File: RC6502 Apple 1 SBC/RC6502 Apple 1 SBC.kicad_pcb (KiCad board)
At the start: 2 copper layers, 99.1 x 99.7 mm, 48 parts, among them J1 VP GND, J10 RAM_EN, J11 PIA_EN, J2 Arduino Nano, J3 Backplane, J4 Hole, J5 Hole, J6 Hole, J7 Hole, J8 Power, J9 ROM_EN, SW1 RESET, U1 WD65C02, U2 HM62256BLP-7, U3 74HCT138, U4 28C256, U5 74HCT00, U6 NE555, U7 74HCT04, U8 WD65C21, U9 MCP23S17, X1 1MHz

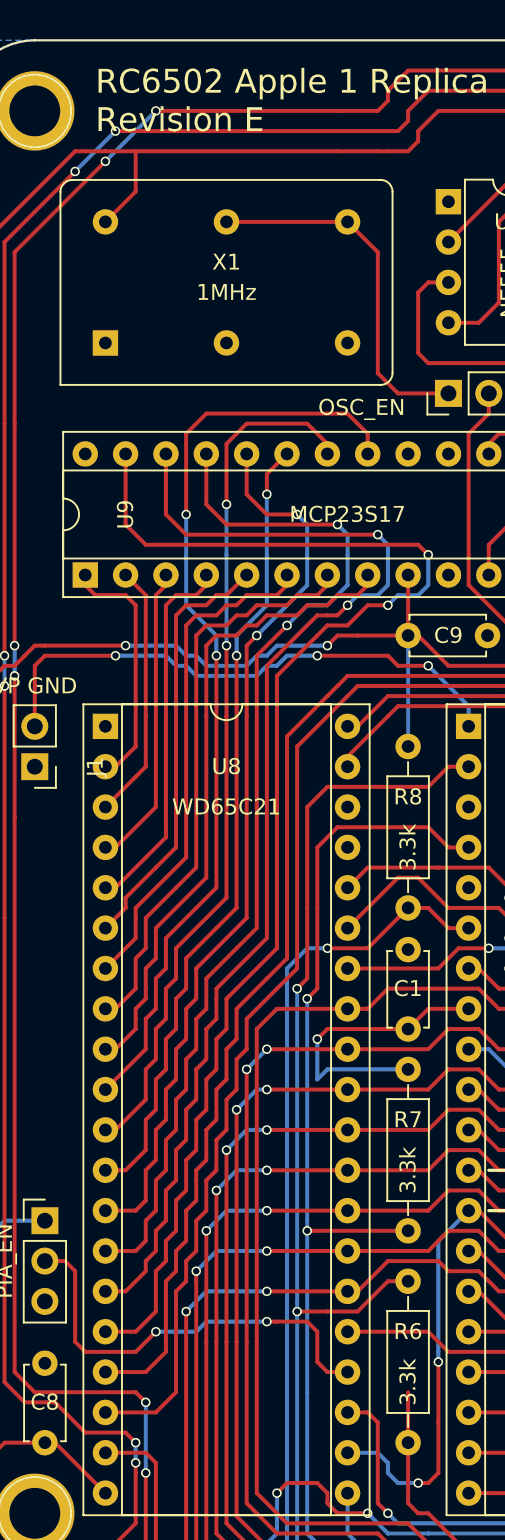
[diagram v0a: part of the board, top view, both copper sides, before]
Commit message: SBC revision E was missing VCC to CPU for some reason
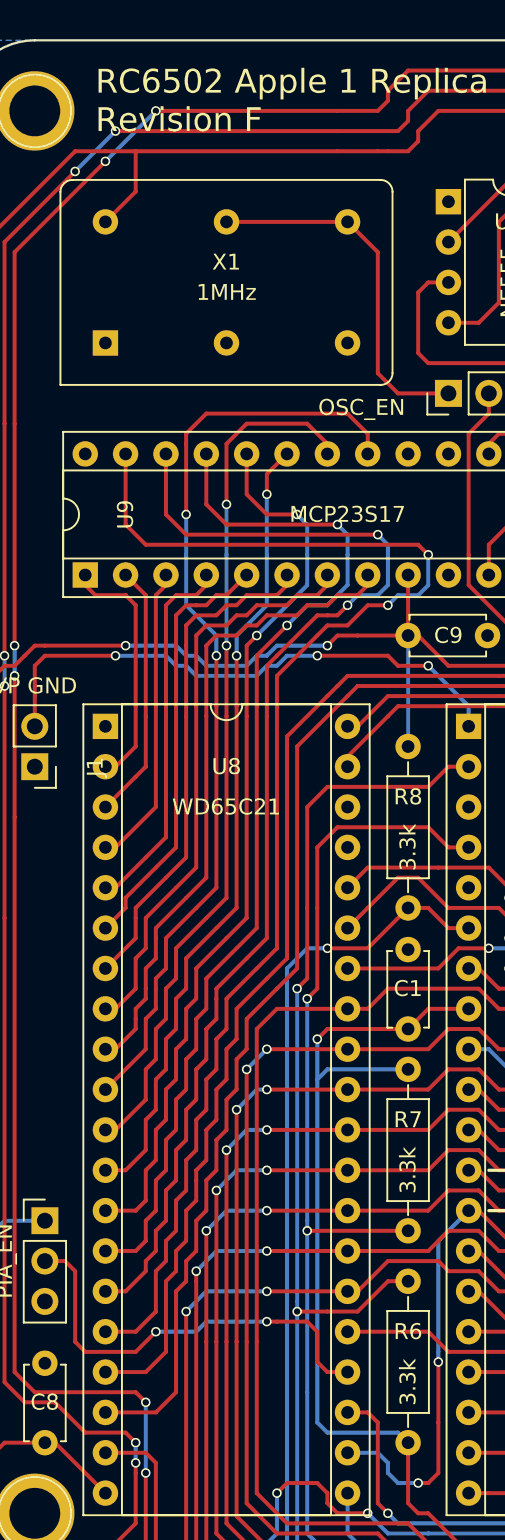
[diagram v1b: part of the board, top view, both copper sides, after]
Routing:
- net VCC: track 643.9 -> 668.5 mm
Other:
- board text added: "RC6502 Apple 1 Replica Revision F"
- board text removed: "RC6502 Apple 1 Replica Revision E"
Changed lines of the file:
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@@
   (general
     (links 240)
-    (no_connects 1)
+    (no_connects 0)
     (area 114.23 35.22 220.820001 148.420001)
     (thickness 1.6)
     (drawings 168)
-    (tracks 2242)
+    (tracks 2245)
     (zones 0)
     (modules 48)
@@
     (effects (font (size 1 1) (thickness 0.15)))
   )
-  (gr_text "RC6502 Apple 1 Replica\nRevision E" (at 124.46 43.18) (layer F.SilkS)
+  (gr_text "RC6502 Apple 1 Replica\nRevision F" (at 124.46 43.18) (layer F.SilkS)
     (effects (font (size 1.5 1.5) (thickness 0.3)) (justify left))
   )
@@
   (segment (start 189.865 67.31) (end 191.135 66.04) (width 0.25) (layer F.Cu) (net 2))
   (segment (start 191.135 66.04) (end 191.135 65.405) (width 0.25) (layer F.Cu) (net 2))
+  (segment (start 138.43 104.775) (end 138.43 126.365) (width 0.25) (layer B.Cu) (net 3))
+  (segment (start 143.51 127) (end 144.145 127.635) (width 0.25) (layer B.Cu) (net 3))
+  (segment (start 139.065 127) (end 143.51 127) (width 0.25) (layer B.Cu) (net 3))
+  (segment (start 138.43 126.365) (end 139.065 127) (width 0.25) (layer B.Cu) (net 3))
   (segment (start 157.48 48.895) (end 158.75 48.895) (width 0.25) (layer F.Cu) (net 3))
   (segment (start 158.75 48.895) (end 164.465 43.18) (width 0.25) (layer F.Cu) (net 3))
@@
   (segment (start 119.38 78.74) (end 118.745 78.74) (width 0.25) (layer F.Cu) (net 3))
   (segment (start 144.145 127.635) (end 144.145 131.445) (width 0.25) (layer F.Cu) (net 3))
-  (segment (start 145.415 132.08) (end 149.225 135.89) (width 0.25) (layer F.Cu) (net 3))
-  (via (at 149.225 135.89) (size 0.6) (drill 0.4) (layers F.Cu B.Cu) (net 3))
-  (segment (start 144.145 131.445) (end 144.78 132.08) (width 0.25) (layer F.Cu) (net 3))
   (segment (start 144.78 132.08) (end 145.415 132.08) (width 0.25) (layer F.Cu) (net 3))
+  (segment (start 144.145 131.445) (end 144.78 132.08) (width 0.25) (layer F.Cu) (net 3))
+  (via (at 149.225 135.89) (size 0.6) (drill 0.4) (layers F.Cu B.Cu) (net 3))
+  (segment (start 145.415 132.08) (end 149.225 135.89) (width 0.25) (layer F.Cu) (net 3))
   (segment (start 174.625 132.715) (end 177.8 132.715) (width 0.25) (layer F.Cu) (net 3))
   (via (at 178.435 134.62) (size 0.6) (drill 0.4) (layers F.Cu B.Cu) (net 3))
@@
   (via (at 138.43 102.235) (size 0.6) (drill 0.4) (layers F.Cu B.Cu) (net 3))
   (segment (start 138.43 102.235) (end 139.065 101.6) (width 0.25) (layer F.Cu) (net 3))
-  (segment (start 144.145 127.635) (end 144.145 124.46) (width 0.25) (layer F.Cu) (net 3))
   (segment (start 144.145 101.6) (end 145.415 100.33) (width 0.25) (layer F.Cu) (net 3))
   (segment (start 145.415 100.33) (end 147.955 100.33) (width 0.25) (layer F.Cu) (net 3))

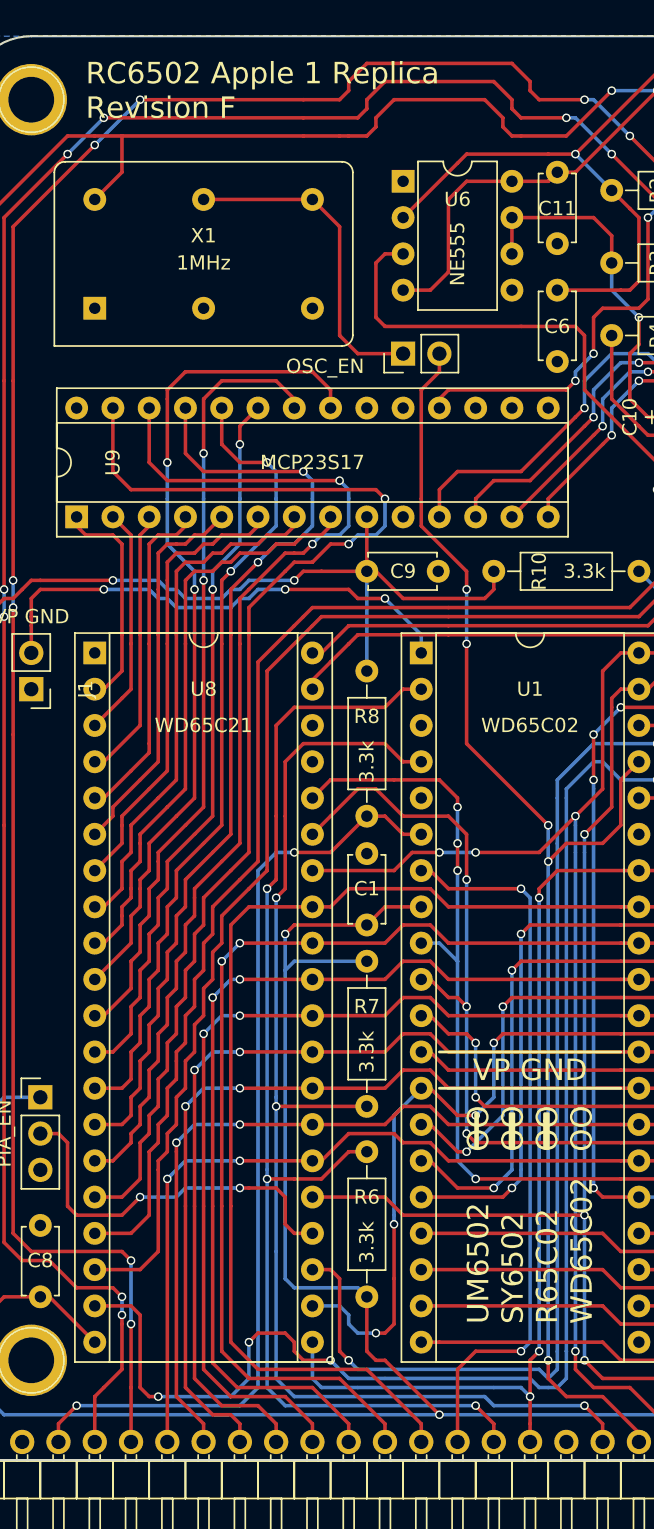
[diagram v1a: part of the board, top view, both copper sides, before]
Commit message: Added Phi1 to backplane connector
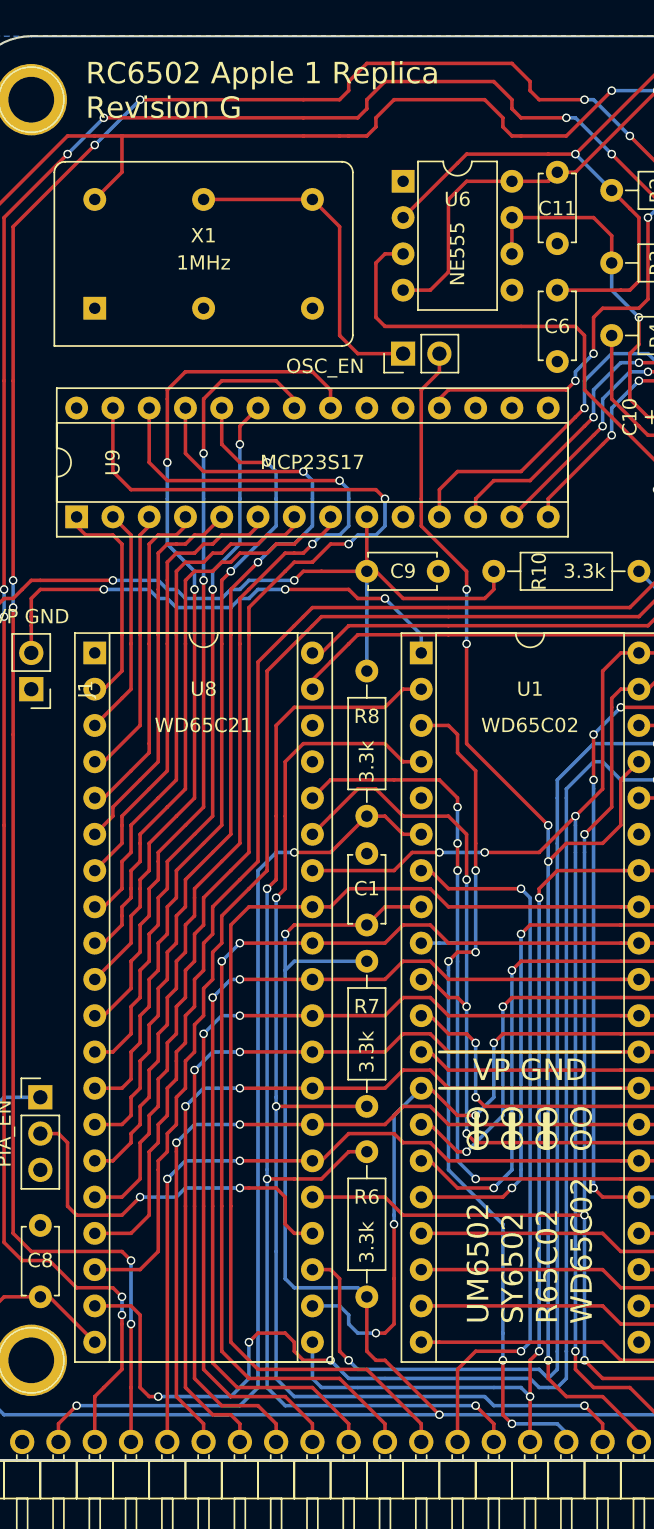
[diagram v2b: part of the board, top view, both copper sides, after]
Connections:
- J3 pad 23: (no net) -> PHI1
- U1 pad 3: (no net) -> PHI1
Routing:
- net PHI1: track 0.00 -> 59.7 mm, vias 0 -> 5
- net A0: track 118.0 -> 117.4 mm
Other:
- board text added: "RC6502 Apple 1 Replica Revision G"
- board text removed: "RC6502 Apple 1 Replica Revision F"
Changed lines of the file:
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@@
 (kicad_pcb (version 4) (host pcbnew 4.0.7)
   (general
-    (links 240)
+    (links 241)
     (no_connects 0)
-    (area 114.23 35.22 220.820001 148.420001)
+    (area 116.129999 39.294999 215.340001 139.140001)
     (thickness 1.6)
     (drawings 168)
-    (tracks 2245)
+    (tracks 2270)
     (zones 0)
     (modules 48)
-    (nets 84)
+    (nets 85)
   )
   (page A4)
@@
   (net 82 "Net-(J11-Pad2)")
   (net 83 "Net-(JP1-Pad1)")
+  (net 84 PHI1)
   (net_class Default "This is the default net class."
     (clearance 0.2)
@@
     (add_net OUT_DA)
     (add_net OUT_RDA)
+    (add_net PHI1)
     (add_net PHI2)
     (add_net P_RESET)
@@
     (pad 22 thru_hole oval (at 15.24 45.72) (size 1.6 1.6) (drill 0.8) (layers *.Cu *.Mask)
       (net 19 A12))
-    (pad 3 thru_hole oval (at 0 5.08) (size 1.6 1.6) (drill 0.8) (layers *.Cu *.Mask))
+    (pad 3 thru_hole oval (at 0 5.08) (size 1.6 1.6) (drill 0.8) (layers *.Cu *.Mask)
+      (net 84 PHI1))
     (pad 23 thru_hole oval (at 15.24 43.18) (size 1.6 1.6) (drill 0.8) (layers *.Cu *.Mask)
       (net 18 A13))
@@
     (pad 22 thru_hole oval (at 0 53.34 270) (size 1.7 1.7) (drill 1) (layers *.Cu *.Mask)
       (net 35 IRQ))
-    (pad 23 thru_hole oval (at 0 55.88 270) (size 1.7 1.7) (drill 1) (layers *.Cu *.Mask))
+    (pad 23 thru_hole oval (at 0 55.88 270) (size 1.7 1.7) (drill 1) (layers *.Cu *.Mask)
+      (net 84 PHI1))
     (pad 24 thru_hole oval (at 0 58.42 270) (size 1.7 1.7) (drill 1) (layers *.Cu *.Mask)
       (net 36 RW))
@@
     (effects (font (size 1 1) (thickness 0.15)))
   )
-  (gr_text "RC6502 Apple 1 Replica\nRevision F" (at 124.46 43.18) (layer F.SilkS)
+  (gr_text "RC6502 Apple 1 Replica\nRevision G" (at 124.46 43.18) (layer F.SilkS)
     (effects (font (size 1.5 1.5) (thickness 0.3)) (justify left))
   )
@@
   (segment (start 175.895 116.205) (end 182.245 116.205) (width 0.25) (layer F.Cu) (net 30))
   (via (at 175.895 116.205) (size 0.6) (drill 0.4) (layers F.Cu B.Cu) (net 30))
+  (segment (start 149.225 102.87) (end 150.495 102.87) (width 0.25) (layer B.Cu) (net 31))
   (segment (start 194.31 128.27) (end 194.31 130.175) (width 0.25) (layer B.Cu) (net 31))
   (segment (start 189.23 132.08) (end 190.5 130.81) (width 0.25) (layer F.Cu) (net 31))
@@
   (segment (start 178.435 117.475) (end 189.865 117.475) (width 0.25) (layer F.Cu) (net 31))
   (segment (start 150.495 97.79) (end 150.495 95.885) (width 0.25) (layer F.Cu) (net 31))
-  (segment (start 150.495 92.71) (end 149.225 91.44) (width 0.25) (layer F.Cu) (net 31))
-  (segment (start 149.225 91.44) (end 146.05 91.44) (width 0.25) (layer F.Cu) (net 31))
-  (segment (start 141.605 91.44) (end 146.05 91.44) (width 0.25) (layer F.Cu) (net 31))
-  (segment (start 140.335 92.71) (end 141.605 91.44) (width 0.25) (layer F.Cu) (net 31))
-  (segment (start 150.495 97.79) (end 150.495 104.14) (width 0.25) (layer B.Cu) (net 31))
-  (via (at 150.495 97.79) (size 0.6) (drill 0.4) (layers F.Cu B.Cu) (net 31))
-  (segment (start 150.495 93.345) (end 150.495 92.71) (width 0.25) (layer F.Cu) (net 31))
-  (via (at 150.495 93.345) (size 0.6) (drill 0.4) (layers F.Cu B.Cu) (net 31))
-  (segment (start 150.495 95.885) (end 150.495 93.345) (width 0.25) (layer B.Cu) (net 31))
   (via (at 150.495 95.885) (size 0.6) (drill 0.4) (layers F.Cu B.Cu) (net 31))
+  (segment (start 150.495 95.885) (end 150.495 93.345) (width 0.25) (layer B.Cu) (net 31))
+  (via (at 150.495 93.345) (size 0.6) (drill 0.4) (layers F.Cu B.Cu) (net 31))
+  (segment (start 150.495 93.345) (end 150.495 92.71) (width 0.25) (layer F.Cu) (net 31))
+  (via (at 150.495 97.79) (size 0.6) (drill 0.4) (layers F.Cu B.Cu) (net 31))
+  (segment (start 150.495 97.79) (end 150.495 102.87) (width 0.25) (layer B.Cu) (net 31))
+  (segment (start 140.335 92.71) (end 141.605 91.44) (width 0.25) (layer F.Cu) (net 31))
+  (segment (start 141.605 91.44) (end 146.05 91.44) (width 0.25) (layer F.Cu) (net 31))
+  (segment (start 149.225 91.44) (end 146.05 91.44) (width 0.25) (layer F.Cu) (net 31))
+  (segment (start 150.495 92.71) (end 149.225 91.44) (width 0.25) (layer F.Cu) (net 31))
+  (segment (start 150.495 102.87) (end 150.495 104.14) (width 0.25) (layer B.Cu) (net 31))
   (segment (start 151.765 119.38) (end 161.925 119.38) (width 0.25) (layer F.Cu) (net 31))
   (via (at 151.765 119.38) (size 0.6) (drill 0.4) (layers F.Cu B.Cu) (net 31))
   (segment (start 151.765 119.38) (end 150.495 118.11) (width 0.25) (layer B.Cu) (net 31))
   (segment (start 150.495 118.11) (end 150.495 104.14) (width 0.25) (layer B.Cu) (net 31))
-  (segment (start 150.495 104.14) (end 149.225 102.87) (width 0.25) (layer B.Cu) (net 31))
   (segment (start 147.955 102.87) (end 149.225 102.87) (width 0.25) (layer B.Cu) (net 31))
   (segment (start 168.275 118.745) (end 169.545 118.745) (width 0.25) (layer F.Cu) (net 31))
@@
   (segment (start 146.05 97.79) (end 147.32 96.52) (width 0.25) (layer F.Cu) (net 33))
   (segment (start 145.415 97.79) (end 140.335 97.79) (width 0.25) (layer F.Cu) (net 33))
-  (via (at 151.765 96.52) (size 0.6) (drill 0.4) (layers F.Cu B.Cu) (net 33))
-  (segment (start 149.225 96.52) (end 151.765 96.52) (width 0.25) (layer B.Cu) (net 33))
+  (via (at 152.4 96.52) (size 0.6) (drill 0.4) (layers F.Cu B.Cu) (net 33))
+  (segment (start 149.225 96.52) (end 152.4 96.52) (width 0.25) (layer B.Cu) (net 33))
   (via (at 149.225 96.52) (size 0.6) (drill 0.4) (layers F.Cu B.Cu) (net 33))
-  (segment (start 151.765 96.52) (end 156.21 96.52) (width 0.25) (layer F.Cu) (net 33))
+  (segment (start 152.4 96.52) (end 156.21 96.52) (width 0.25) (layer F.Cu) (net 33))
   (segment (start 158.75 94.615) (end 158.75 93.98) (width 0.25) (layer B.Cu) (net 33))
   (segment (start 163.195 82.55) (end 161.925 82.55) (width 0.25) (layer F.Cu) (net 33))
@@
   (segment (start 142.24 60.325) (end 142.24 52.705) (width 0.25) (layer F.Cu) (net 83))
   (segment (start 132.715 50.8) (end 140.335 50.8) (width 0.25) (layer F.Cu) (net 83))
+  (segment (start 149.86 104.775) (end 149.86 104.14) (width 0.25) (layer B.Cu) (net 84))
+  (segment (start 153.67 130.175) (end 153.67 122.555) (width 0.25) (layer B.Cu) (net 84))
+  (segment (start 153.67 132.08) (end 153.67 130.175) (width 0.25) (layer B.Cu) (net 84))
+  (via (at 153.67 132.08) (size 0.6) (drill 0.4) (layers F.Cu B.Cu) (net 84))
+  (segment (start 153.67 135.89) (end 153.67 132.08) (width 0.25) (layer F.Cu) (net 84))
+  (segment (start 154.305 136.525) (end 153.67 135.89) (width 0.25) (layer F.Cu) (net 84))
+  (via (at 154.305 136.525) (size 0.6) (drill 0.4) (layers F.Cu B.Cu) (net 84))
+  (segment (start 157.48 136.525) (end 154.305 136.525) (width 0.25) (layer B.Cu) (net 84))
+  (segment (start 158.115 137.16) (end 157.48 136.525) (width 0.25) (layer B.Cu) (net 84) (status 400000))
+  (segment (start 153.67 122.555) (end 149.86 118.745) (width 0.25) (layer B.Cu) (net 84))
+  (segment (start 149.86 104.775) (end 149.86 118.745) (width 0.25) (layer B.Cu) (net 84))
+  (via (at 151.765 97.79) (size 0.6) (drill 0.4) (layers F.Cu B.Cu) (net 84))
+  (segment (start 151.765 97.79) (end 151.765 103.505) (width 0.25) (layer B.Cu) (net 84))
+  (segment (start 149.86 87.63) (end 147.955 87.63) (width 0.25) (layer F.Cu) (net 84) (status 800000))
+  (segment (start 151.765 90.805) (end 151.765 95.885) (width 0.25) (layer F.Cu) (net 84))
+  (segment (start 150.495 89.535) (end 151.765 90.805) (width 0.25) (layer F.Cu) (net 84))
+  (segment (start 150.495 88.265) (end 150.495 89.535) (width 0.25) (layer F.Cu) (net 84))
+  (segment (start 149.86 87.63) (end 150.495 88.265) (width 0.25) (layer F.Cu) (net 84))
+  (segment (start 151.765 95.885) (end 151.765 97.79) (width 0.25) (layer F.Cu) (net 84))
+  (via (at 151.765 103.505) (size 0.6) (drill 0.4) (layers F.Cu B.Cu) (net 84))
+  (segment (start 150.495 103.505) (end 151.765 103.505) (width 0.25) (layer F.Cu) (net 84))
+  (segment (start 149.86 104.14) (end 150.495 103.505) (width 0.25) (layer F.Cu) (net 84))
+  (via (at 149.86 104.14) (size 0.6) (drill 0.4) (layers F.Cu B.Cu) (net 84))
+  (segment (start 158.115 137.795) (end 158.115 137.16) (width 0.25) (layer B.Cu) (net 84) (status C00000))
   (zone (net 1) (net_name GND) (layer B.Cu) (hatch edge 0.508)
     (connect_pads (clearance 0.508))

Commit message: Cleaned up SBC schematic
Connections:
- J2 pad 9: (no net) -> CLOCK
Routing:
- net CLOCK: track 95.6 -> 156.2 mm, vias 5 -> 14
- net TX: track 172.3 -> 171.6 mm
- net Net-(J2-Pad16): track 77.3 -> 78.0 mm
- net Net-(J2-Pad14): track 73.1 -> 72.6 mm
